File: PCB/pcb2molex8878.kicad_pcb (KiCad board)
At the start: 2 copper layers, 16.3 x 37.3 mm, 1 part, among them J1 Molex_DIP28_edge_contacts

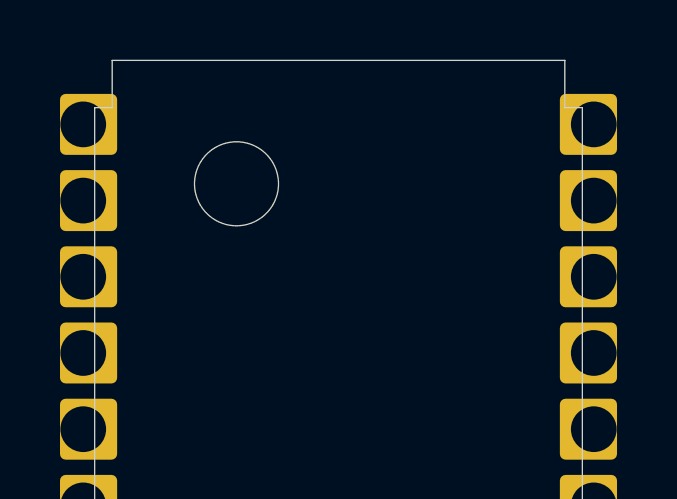
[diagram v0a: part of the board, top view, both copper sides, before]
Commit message: make polarity hole even# of mils, add gerbers
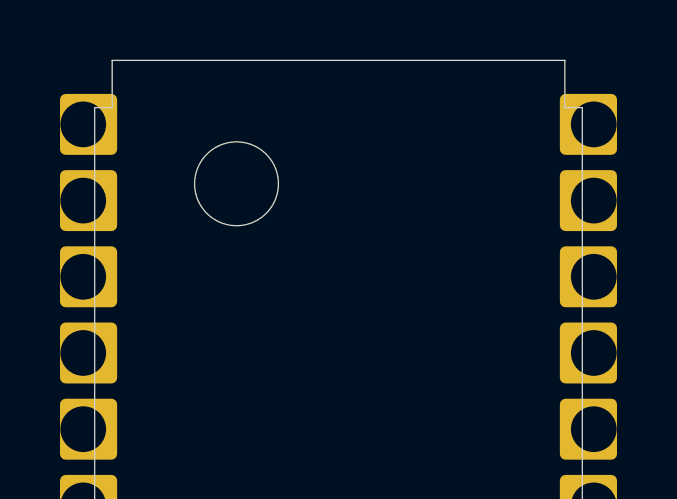
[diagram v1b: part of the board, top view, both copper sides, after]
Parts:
- removed J1: Molex_DIP28_edge_contacts, 000_LOCAL:pcb2molex8878
- added J?: Molex_50-39-5288, 000_LOCAL:pcb2molex8878, F.Cu at (147.2, 99.2)
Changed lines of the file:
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@@
-(kicad_pcb (version 20171130) (host pcbnew 5.1.3-ffb9f22~84~ubuntu19.04.1)
+(kicad_pcb (version 20171130) (host pcbnew 5.1.4-e60b266~84~ubuntu19.04.1)
   (general
     (thickness 1.6)
@@
     (38 B.Mask user)
     (39 F.Mask user)
-    (40 Dwgs.User user hide)
-    (41 Cmts.User user hide)
-    (42 Eco1.User user hide)
-    (43 Eco2.User user hide)
+    (40 Dwgs.User user)
+    (41 Cmts.User user)
+    (42 Eco1.User user)
+    (43 Eco2.User user)
     (44 Edge.Cuts user)
     (45 Margin user hide)
@@
     (visible_elements FFFFFF7F)
     (pcbplotparams
-      (layerselection 0x010fc_ffffffff)
+      (layerselection 0x01ffc_ffffffff)
       (usegerberextensions false)
       (usegerberattributes false)
@@
       (creategerberjobfile false)
       (excludeedgelayer true)
-      (linewidth 0.100000)
+      (linewidth 0.050800)
       (plotframeref false)
       (viasonmask false)
@@
       (outputformat 1)
       (mirror false)
-      (drillshape 1)
+      (drillshape 0)
       (scaleselection 1)
-      (outputdirectory ""))
+      (outputdirectory "gerber/"))
   )
   (net 0 "")
@@
     (at 147.2184 99.187)
     (descr "Castellated edge contacts to fit Molex 8878 Socket")
-    (fp_text reference J1 (at -0.6604 1.1176 -90) (layer Dwgs.User) hide
+    (fp_text reference J? (at -0.9906 -0.9906 -90) (layer Dwgs.User) hide
       (effects (font (size 1.2065 1.2065) (thickness 0.127)) (justify left bottom))
     )
-    (fp_text value Molex_DIP28_edge_contacts (at 2.4003 -6.7691 -90) (layer F.Fab) hide
+    (fp_text value Molex_50-39-5288 (at 2.0701 -8.8773 -90) (layer F.Fab) hide
       (effects (font (size 1.2065 1.2065) (thickness 0.1016)) (justify left bottom))
     )
-    (fp_text user thingiverse.com/thing:3723135 (at 0.3302 16.1082) (layer Eco2.User)
+    (fp_text user thingiverse.com/thing:3723135 (at 0.025 14.45 unlocked) (layer Eco2.User)
       (effects (font (size 0.2 0.2) (thickness 0.01)))
     )
-    (fp_text user "back components & legs" (at -0.9198 12.3582) (layer Dwgs.User)
+    (fp_text user "back components & legs" (at -1.25 10.25) (layer Dwgs.User)
       (effects (font (size 0.2 0.2) (thickness 0.01)))
     )
@@
     (fp_line (start -6.25 10) (end -6 10.25) (layer Dwgs.User) (width 0.01))
     (fp_line (start -6 9.75) (end -6.25 10) (layer Dwgs.User) (width 0.01))
-    (fp_text user "12.5x36x1.3mm pocket" (at -0.9198 12.1082) (layer Dwgs.User)
+    (fp_text user "12.5x36x1.2mm pocket" (at -1.25 10) (layer Dwgs.User)
       (effects (font (size 0.2 0.2) (thickness 0.01)))
     )
@@
     (fp_line (start 7.5565 18.6436) (end 7.5565 17.0688) (layer Eco2.User) (width 0.01))
     (fp_line (start -7.5565 18.6436) (end 7.5565 18.6436) (layer Eco2.User) (width 0.01))
-    (fp_text user "not the actual final dimansions in some places." (at 0.4802 18.9832) (layer Dwgs.User)
+    (fp_text user "not the actual final dimensions in some places." (at 0.15 16.875 unlocked) (layer Dwgs.User)
       (effects (font (size 0.2 0.2) (thickness 0.01)))
     )
-    (fp_text user "including allowance for 0.034\" mill radius," (at 0.4552 18.4332) (layer Dwgs.User)
+    (fp_text user "including allowance for 0.034\" mill radius," (at 0.125 16.325 unlocked) (layer Dwgs.User)
       (effects (font (size 0.2 0.2) (thickness 0.01)))
     )
-    (fp_text user "Edge cuts reflect the necessary router path," (at 0.4302 17.7832) (layer Dwgs.User)
+    (fp_text user "Edge.Cuts reflects the necessary router path," (at 0.1 15.675 unlocked) (layer Dwgs.User)
       (effects (font (size 0.2 0.2) (thickness 0.01)))
     )
-    (fp_text user "May delete NPTH mechanical polarity hole." (at 0.3302 14.8582) (layer Eco1.User)
+    (fp_text user "May delete NPTH mechanical polarity hole." (at 0 12.75) (layer Eco1.User)
       (effects (font (size 0.2 0.2) (thickness 0.01)))
     )
-    (fp_text user "Eco1.User is Edge.Cuts for use without carrier." (at 0.3004 14.3582) (layer Eco1.User)
+    (fp_text user "Eco1.User is Edge.Cuts for use without carrier." (at -0.0298 12.25) (layer Eco1.User)
       (effects (font (size 0.2 0.2) (thickness 0.01)))
     )
@@
     (fp_arc (start 8.4201 17.9324) (end 8.4201 17.0688) (angle -90) (layer Dwgs.User) (width 0.00508))
     (fp_arc (start -8.4201 17.9324) (end -7.5565 17.9324) (angle -90) (layer Dwgs.User) (width 0.00508))
-    (fp_text user "Eco2.User is Edge.Cuts for use with" (at 0.4052 15.6082) (layer Eco2.User)
+    (fp_text user "Eco2.User is Edge.Cuts for use with" (at 0.125 14.025 unlocked) (layer Eco2.User)
       (effects (font (size 0.2 0.2) (thickness 0.01)))
     )
@@
     (fp_line (start -4.5593 19.05) (end -8.128 19.05) (layer Eco1.User) (width 0.0254))
     (fp_line (start 8.128 19.05) (end 4.5593 19.05) (layer Eco1.User) (width 0.0254))
-    (pad "" np_thru_hole circle (at -3.4 -14.53) (size 2.8 2.8) (drill 2.8) (layers *.Cu *.Mask))
+    (pad "" np_thru_hole circle (at -3.4 -14.53) (size 2.794 2.794) (drill 2.794) (layers *.Cu *.Mask))
     (pad 1 thru_hole roundrect (at -8.509 -16.51) (size 1.905 2.032) (drill 1.524 (offset 0.1778 0)) (layers *.Cu *.Mask) (roundrect_rratio 0.1)
       (solder_mask_margin -0.3556))

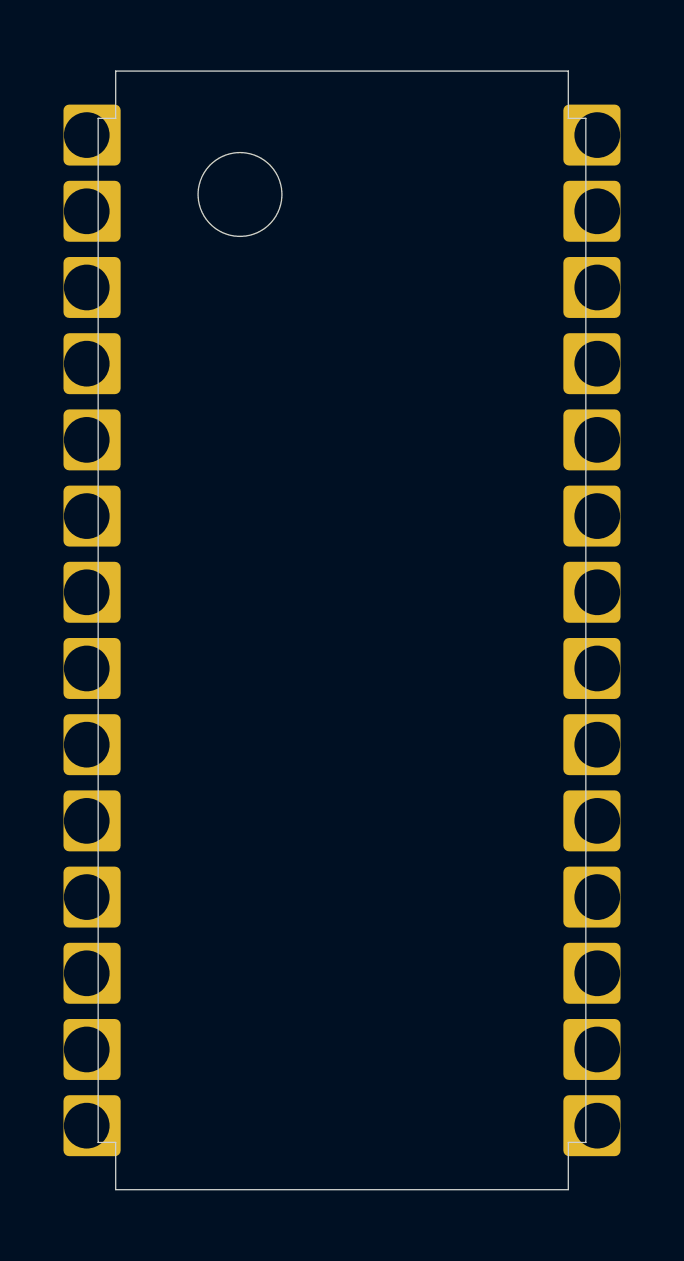
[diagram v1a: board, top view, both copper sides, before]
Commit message: Simple rectangle pcb Larger pcb Further optimized edge contacts footprint Smaller polarity pin & hole Parametric OpenSCAD model for carrier redraw from scratch
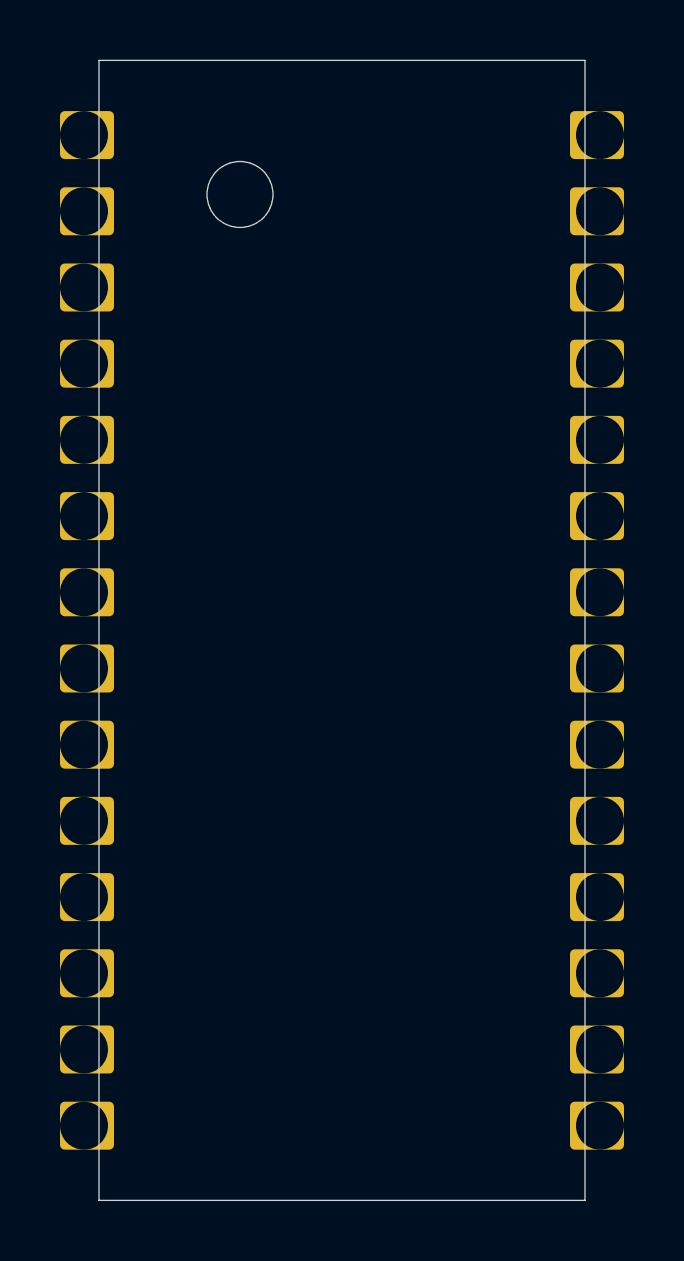
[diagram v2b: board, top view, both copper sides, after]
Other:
- board size 16.3 x 37.3 mm -> 16.2 x 38 mm
